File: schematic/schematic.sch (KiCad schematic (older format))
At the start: 19 parts, among them J1 Conn_01x04, J2 Conn_01x04, J3 Conn_01x04, J4 Conn_01x04, J5 Conn_01x04, SW1 SW_Push_Dual, U1 STM32F401VETx, Y1 Crystal_GND24

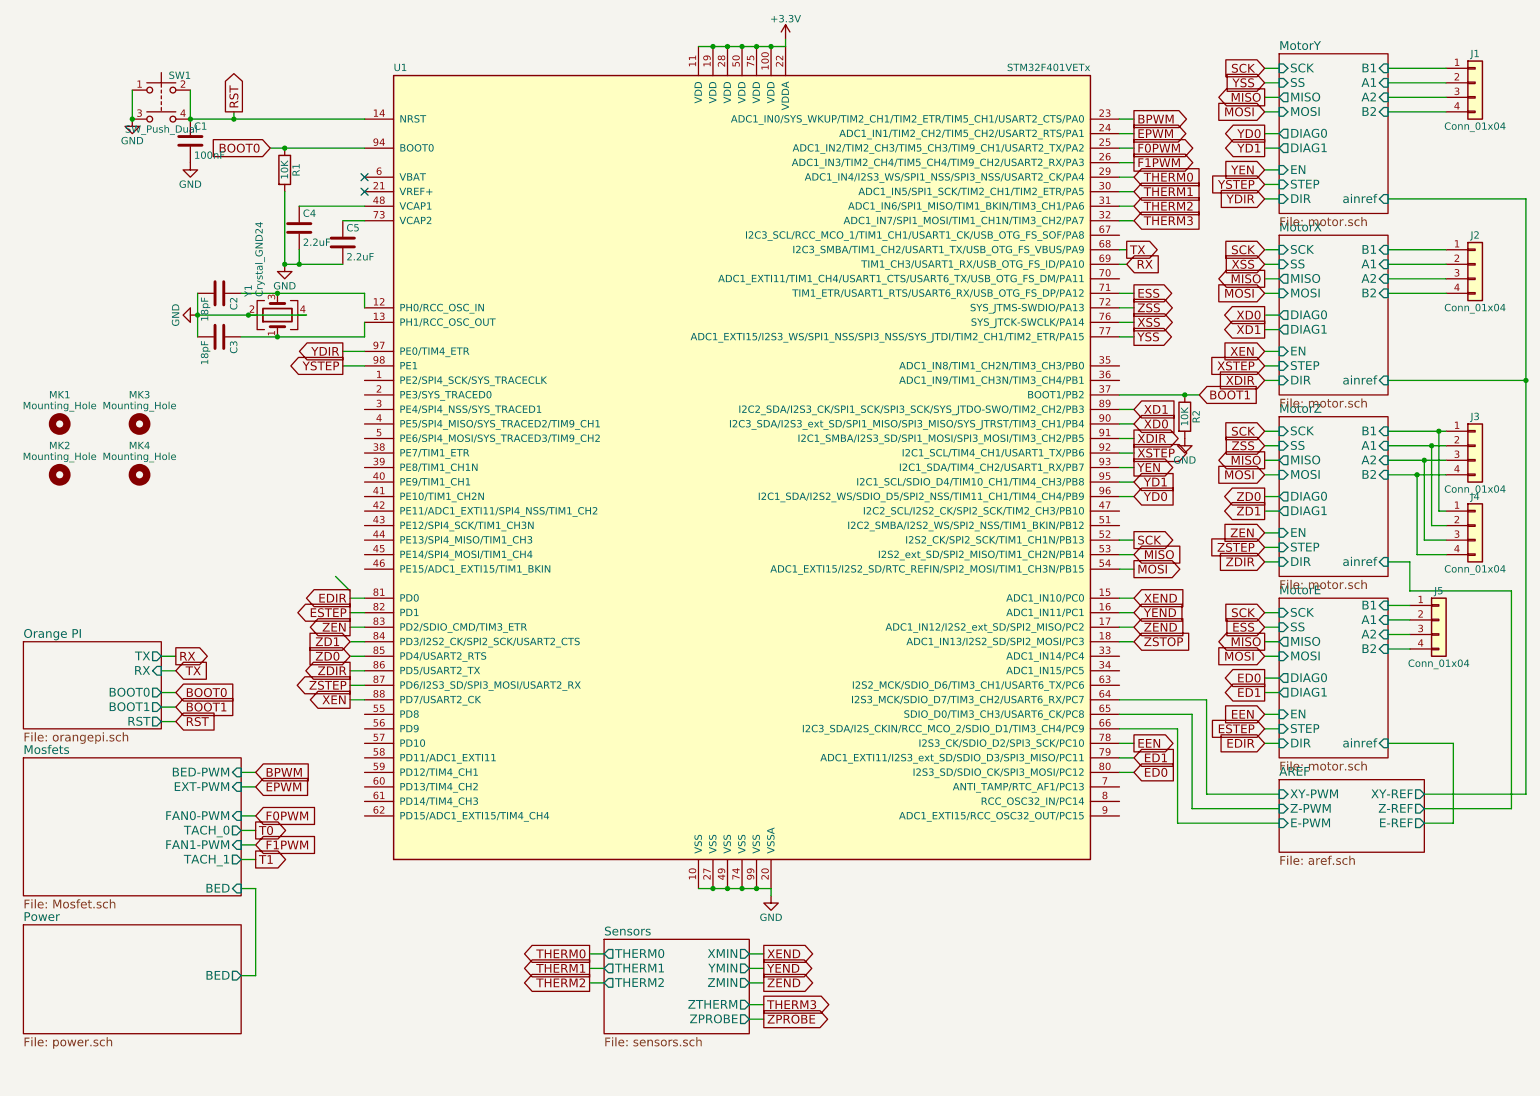
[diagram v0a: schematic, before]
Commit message: routed 3.3V power and start re arange signals
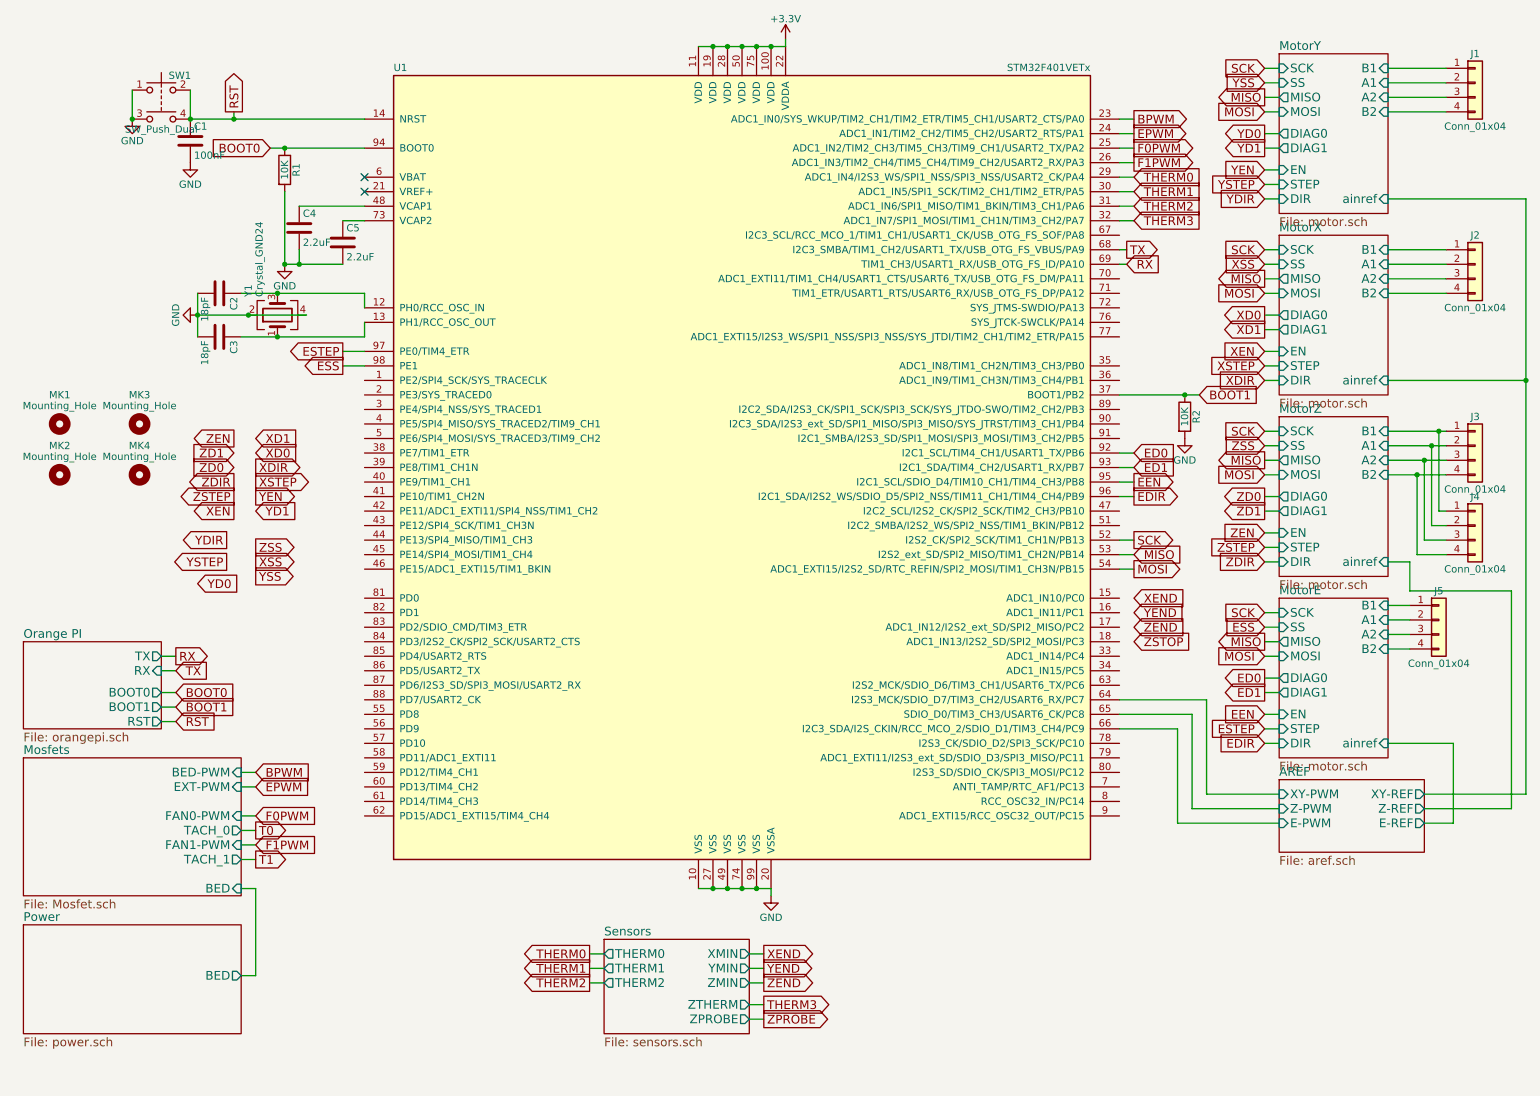
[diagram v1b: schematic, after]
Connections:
- net ED0: now also U1.92 (I2C1_SCL/TIM4_CH1/USART1_TX/PB6); no longer U1.80 (I2S3_SD/SDIO_CK/SPI3_MOSI/PC12)
- net ED1: now also U1.93 (I2C1_SDA/TIM4_CH2/USART1_RX/PB7); no longer U1.79 (ADC1_EXTI11/I2S3_ext_SD/SDIO_D3/SPI3_MISO/PC11)
- net EDIR: now also U1.96 (I2C1_SDA/I2S2_WS/SDIO_D5/SPI2_NSS/TIM11_CH1/TIM4_CH4/PB9); no longer U1.81 (PD0)
- net EEN: now also U1.95 (I2C1_SCL/SDIO_D4/TIM10_CH1/TIM4_CH3/PB8); no longer U1.78 (I2S3_CK/SDIO_D2/SPI3_SCK/PC10)
- net ESS: now also U1.98 (PE1); no longer U1.71 (TIM1_ETR/USART1_RTS/USART6_RX/USB_OTG_FS_DP/PA12)
- net ESTEP: now also U1.97 (PE0/TIM4_ETR); no longer U1.82 (PD1)
- net XD0: no longer U1.90 (I2C3_SDA/I2S3_ext_SD/SPI1_MISO/SPI3_MISO/SYS_JTRST/TIM3_CH1/PB4)
- net XD1: no longer U1.89 (I2C2_SDA/I2S3_CK/SPI1_SCK/SPI3_SCK/SYS_JTDO-SWO/TIM2_CH2/PB3)
- net XDIR: no longer U1.91 (I2C1_SMBA/I2S3_SD/SPI1_MOSI/SPI3_MOSI/TIM3_CH2/PB5)
- net XEN: no longer U1.88 (PD7/USART2_CK)
- net XEND: no longer U1.15 (ADC1_IN10/PC0)
- net XSS: no longer U1.76 (SYS_JTCK-SWCLK/PA14)
- net XSTEP: no longer U1.92 (I2C1_SCL/TIM4_CH1/USART1_TX/PB6)
- net YD0: no longer U1.96 (I2C1_SDA/I2S2_WS/SDIO_D5/SPI2_NSS/TIM11_CH1/TIM4_CH4/PB9)
- net YD1: no longer U1.95 (I2C1_SCL/SDIO_D4/TIM10_CH1/TIM4_CH3/PB8)
- net YDIR: no longer U1.97 (PE0/TIM4_ETR)
- net YEN: no longer U1.93 (I2C1_SDA/TIM4_CH2/USART1_RX/PB7)
- net YEND: no longer U1.16 (ADC1_IN11/PC1)
- net YSS: no longer U1.77 (ADC1_EXTI15/I2S3_WS/SPI1_NSS/SPI3_NSS/SYS_JTDI/TIM2_CH1/TIM2_ETR/PA15)
- net YSTEP: no longer U1.98 (PE1)
- net ZD0: no longer U1.85 (PD4/USART2_RTS)
- net ZD1: no longer U1.84 (PD3/I2S2_CK/SPI2_SCK/USART2_CTS)
- net ZDIR: no longer U1.86 (PD5/USART2_TX)
- net ZEN: no longer U1.83 (PD2/SDIO_CMD/TIM3_ETR)
- net ZEND: no longer U1.17 (ADC1_IN12/I2S2_ext_SD/SPI2_MISO/PC2)
- net ZSS: no longer U1.72 (SYS_JTMS-SWDIO/PA13)
- net ZSTEP: no longer U1.87 (PD6/I2S3_SD/SPI3_MOSI/USART2_RX)
- net ZSTOP: no longer U1.18 (ADC1_IN13/I2S2_SD/SPI2_MOSI/PC3)
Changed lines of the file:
@@
 LIBS:psmn1
 LIBS:tmc2130
+LIBS:schematic-cache
 EELAYER 25 0
 EELAYER END
@@
 Text GLabel 9100 1600 0    60   Input ~ 0
 YSTEP
-Text GLabel 2750 2850 0    60   Output ~ 0
+Text GLabel 1950 4200 0    60   Output ~ 0
 YSTEP
 Wire Wire Line
-	2900 2850 2750 2850
-Wire Wire Line
 	9100 1600 9200 1600
-Text GLabel 2750 2750 0    60   Output ~ 0
+Text GLabel 1950 4050 0    60   Output ~ 0
 YDIR
 Text GLabel 9100 1700 0    60   Input ~ 0
@@
 Wire Wire Line
 	9200 1700 9100 1700
-Wire Wire Line
-	2900 2750 2750 2750
 Text GLabel 9100 1250 0    60   Output ~ 0
 YD0
@@
 Wire Wire Line
 	9100 1250 9200 1250
-Text GLabel 8200 3750 2    60   Input ~ 0
+Text GLabel 1750 4350 2    60   Input ~ 0
 YD0
-Text GLabel 8200 3650 2    60   Input ~ 0
+Text GLabel 2150 3850 2    60   Input ~ 0
 YD1
-Text GLabel 8200 3550 2    60   Output ~ 0
+Text GLabel 2150 3750 2    60   Output ~ 0
 YEN
-Wire Wire Line
-	8100 3550 8200 3550
-Wire Wire Line
-	8100 3650 8200 3650
-Wire Wire Line
-	8100 3750 8200 3750
 Text GLabel 9100 2750 0    60   Input ~ 0
 XEN
@@
 Wire Wire Line
 	9100 3850 9200 3850
-Text GLabel 8200 3450 2    60   Output ~ 0
+Text GLabel 2150 3650 2    60   Output ~ 0
 XSTEP
-Text GLabel 8200 3350 2    60   Output ~ 0
+Text GLabel 2150 3550 2    60   Output ~ 0
 XDIR
-Text GLabel 8200 3250 2    60   Input ~ 0
+Text GLabel 2150 3450 2    60   Input ~ 0
 XD0
-Text GLabel 8200 3150 2    60   Input ~ 0
+Text GLabel 2150 3350 2    60   Input ~ 0
 XD1
-Text GLabel 2800 5150 0    60   Output ~ 0
+Text GLabel 2000 3850 0    60   Output ~ 0
 XEN
-Wire Wire Line
-	8100 3450 8200 3450
-Wire Wire Line
-	8100 3350 8200 3350
-Wire Wire Line
-	8100 3250 8200 3250
-Wire Wire Line
-	8100 3150 8200 3150
-Wire Wire Line
-	2800 5150 2900 5150
-Text GLabel 2800 5050 0    60   Output ~ 0
+Text GLabel 2000 3750 0    60   Output ~ 0
 ZSTEP
-Text GLabel 2800 4950 0    60   Output ~ 0
+Text GLabel 2000 3650 0    60   Output ~ 0
 ZDIR
-Text GLabel 2800 4850 0    60   Input ~ 0
+Text GLabel 2000 3550 0    60   Input ~ 0
 ZD0
-Text GLabel 2800 4750 0    60   Input ~ 0
+Text GLabel 2000 3450 0    60   Input ~ 0
 ZD1
-Text GLabel 2800 4650 0    60   Output ~ 0
+Text GLabel 2000 3350 0    60   Output ~ 0
 ZEN
-Wire Wire Line
-	2800 5050 2900 5050
-Wire Wire Line
-	2800 4950 2900 4950
-Wire Wire Line
-	2800 4850 2900 4850
-Wire Wire Line
-	2800 4750 2900 4750
-Wire Wire Line
-	2800 4650 2900 4650
-Text GLabel 2800 4550 0    60   Output ~ 0
+Text GLabel 2750 2750 0    60   Output ~ 0
 ESTEP
-Text GLabel 2800 4450 0    60   Output ~ 0
+Text GLabel 8200 3750 2    60   Output ~ 0
 EDIR
-Text GLabel 8200 5650 2    60   Input ~ 0
+Text GLabel 8200 3450 2    60   Input ~ 0
 ED0
-Text GLabel 8200 5550 2    60   Input ~ 0
+Text GLabel 8200 3550 2    60   Input ~ 0
 ED1
-Text GLabel 8200 5450 2    60   Output ~ 0
+Text GLabel 8200 3650 2    60   Output ~ 0
 EEN
-Wire Wire Line
-	8100 5650 8200 5650
-Wire Wire Line
-	8100 5550 8200 5550
-Wire Wire Line
-	8100 5450 8200 5450
-Wire Wire Line
-	2800 4450 2900 4450
-Wire Wire Line
-	2800 4550 2900 4550
 Wire Wire Line
 	2050 6450 2150 6450
@@
 Wire Wire Line
 	8100 4250 8200 4250
-Text GLabel 8200 2650 2    60   Output ~ 0
+Text GLabel 2150 4300 2    60   Output ~ 0
 YSS
-Text GLabel 8200 2550 2    60   Output ~ 0
+Text GLabel 2150 4200 2    60   Output ~ 0
 XSS
-Text GLabel 8200 2450 2    60   Output ~ 0
+Text GLabel 2150 4100 2    60   Output ~ 0
 ZSS
-Text GLabel 8200 2350 2    60   Output ~ 0
+Text GLabel 2750 2850 0    60   Output ~ 0
 ESS
-Wire Wire Line
-	8100 2650 8200 2650
-Wire Wire Line
-	8100 2550 8200 2550
-Wire Wire Line
-	8100 2450 8200 2450
-Wire Wire Line
-	8100 2350 8200 2350
 Wire Wire Line
 	8100 5150 8700 5150
@@
 Text GLabel 8200 4750 2    60   Input ~ 0
 ZSTOP
-Wire Wire Line
-	8100 4450 8200 4450
-Wire Wire Line
-	8100 4550 8200 4550
-Wire Wire Line
-	8100 4650 8200 4650
-Wire Wire Line
-	8100 4750 8200 4750
 Text GLabel 5650 6900 2    60   Output ~ 0
 XEND
@@
 	1750 2500 2500 2500
 Connection ~ 2100 2500
-Entry Wire Line
-	2700 4300 2800 4400
+Wire Wire Line
+	2900 2850 2750 2850
+Wire Wire Line
+	2750 2750 2900 2750
+Wire Wire Line
+	8100 3750 8200 3750
+Wire Wire Line
+	8100 3650 8200 3650
+Wire Wire Line
+	8200 3550 8100 3550
+Wire Wire Line
+	8100 3450 8200 3450
 $EndSCHEMATC

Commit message: Reassigned signals to driver for easier routing
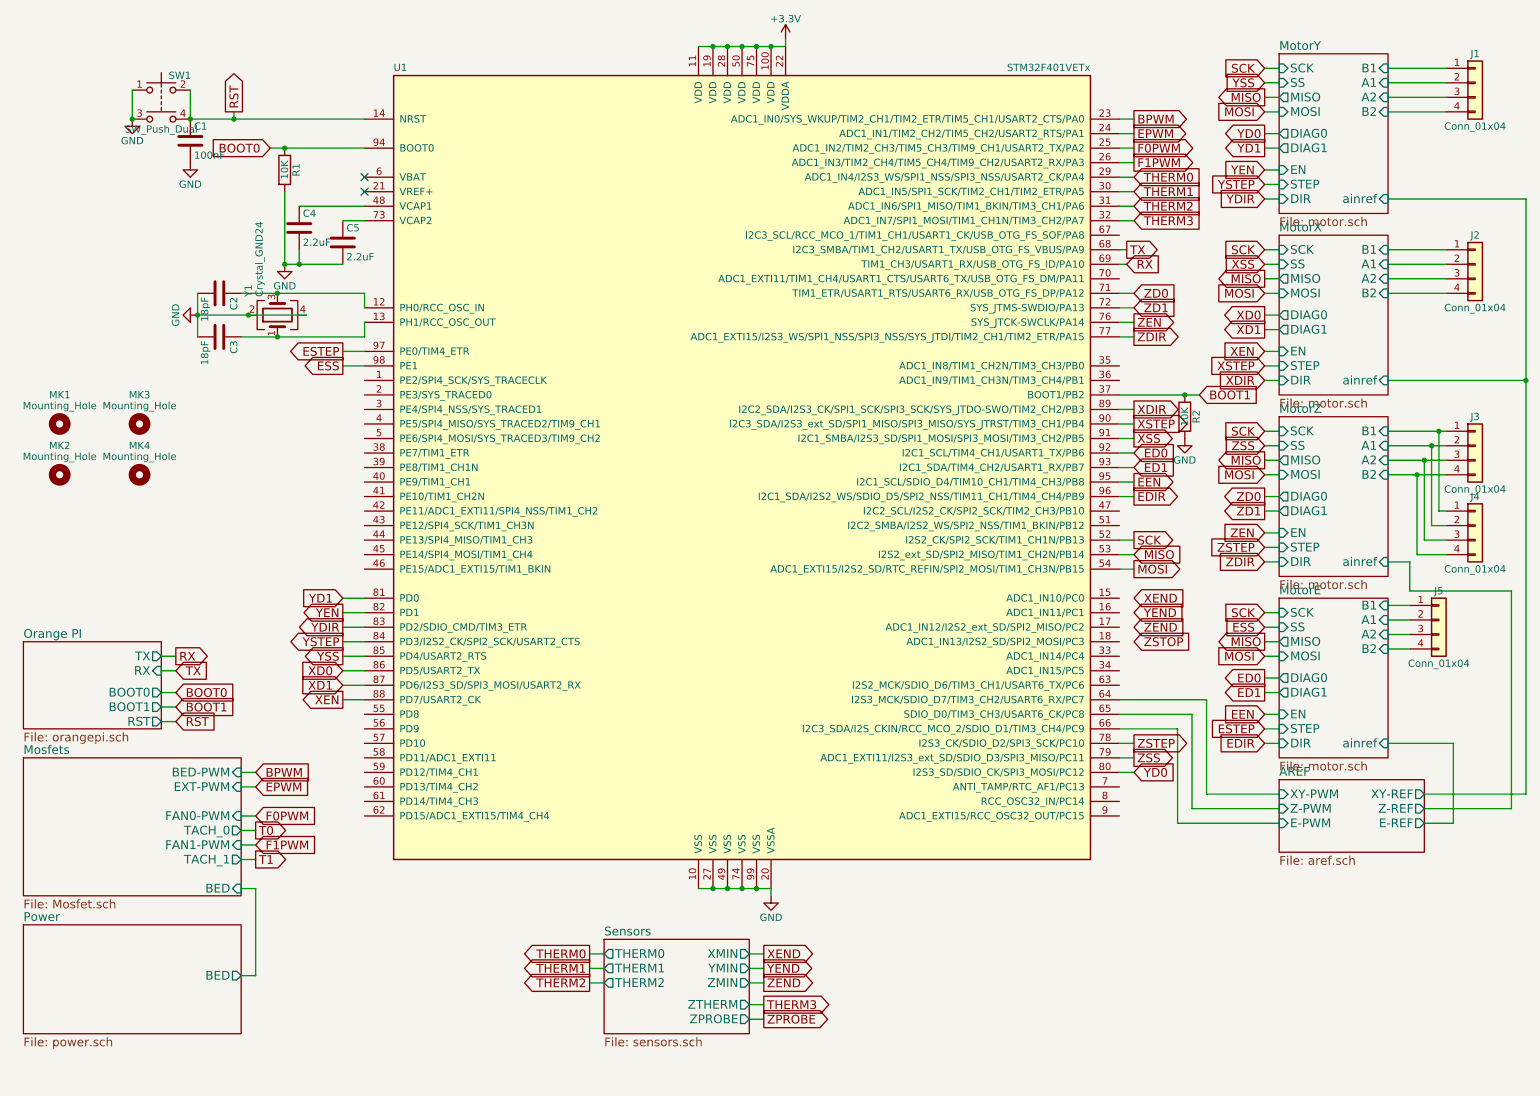
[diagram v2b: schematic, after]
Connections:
- net XD0: now also U1.86 (PD5/USART2_TX)
- net XD1: now also U1.87 (PD6/I2S3_SD/SPI3_MOSI/USART2_RX)
- net XDIR: now also U1.89 (I2C2_SDA/I2S3_CK/SPI1_SCK/SPI3_SCK/SYS_JTDO-SWO/TIM2_CH2/PB3)
- net XEN: now also U1.88 (PD7/USART2_CK)
- net XSS: now also U1.91 (I2C1_SMBA/I2S3_SD/SPI1_MOSI/SPI3_MOSI/TIM3_CH2/PB5)
- net XSTEP: now also U1.90 (I2C3_SDA/I2S3_ext_SD/SPI1_MISO/SPI3_MISO/SYS_JTRST/TIM3_CH1/PB4)
- net YD0: now also U1.80 (I2S3_SD/SDIO_CK/SPI3_MOSI/PC12)
- net YD1: now also U1.81 (PD0)
- net YDIR: now also U1.83 (PD2/SDIO_CMD/TIM3_ETR)
- net YEN: now also U1.82 (PD1)
- net YSS: now also U1.85 (PD4/USART2_RTS)
- net YSTEP: now also U1.84 (PD3/I2S2_CK/SPI2_SCK/USART2_CTS)
- net ZD0: now also U1.71 (TIM1_ETR/USART1_RTS/USART6_RX/USB_OTG_FS_DP/PA12)
- net ZD1: now also U1.72 (SYS_JTMS-SWDIO/PA13)
- net ZDIR: now also U1.77 (ADC1_EXTI15/I2S3_WS/SPI1_NSS/SPI3_NSS/SYS_JTDI/TIM2_CH1/TIM2_ETR/PA15)
- net ZEN: now also U1.76 (SYS_JTCK-SWCLK/PA14)
- net ZSS: now also U1.79 (ADC1_EXTI11/I2S3_ext_SD/SDIO_D3/SPI3_MISO/PC11)
- net ZSTEP: now also U1.78 (I2S3_CK/SDIO_D2/SPI3_SCK/PC10)
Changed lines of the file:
@@
 Text GLabel 9100 1600 0    60   Input ~ 0
 YSTEP
-Text GLabel 1950 4200 0    60   Output ~ 0
+Text GLabel 2750 4750 0    60   Output ~ 0
 YSTEP
 Wire Wire Line
 	9100 1600 9200 1600
-Text GLabel 1950 4050 0    60   Output ~ 0
+Text GLabel 2750 4650 0    60   Output ~ 0
 YDIR
 Text GLabel 9100 1700 0    60   Input ~ 0
@@
 Wire Wire Line
 	9100 1250 9200 1250
-Text GLabel 1750 4350 2    60   Input ~ 0
+Text GLabel 8200 5650 2    60   Input ~ 0
 YD0
-Text GLabel 2150 3850 2    60   Input ~ 0
+Text GLabel 2750 4450 0    60   Input ~ 0
 YD1
-Text GLabel 2150 3750 2    60   Output ~ 0
+Text GLabel 2750 4550 0    60   Output ~ 0
 YEN
 Text GLabel 9100 2750 0    60   Input ~ 0
@@
 Wire Wire Line
 	9100 3850 9200 3850
-Text GLabel 2150 3650 2    60   Output ~ 0
+Text GLabel 8200 3250 2    60   Output ~ 0
 XSTEP
-Text GLabel 2150 3550 2    60   Output ~ 0
+Text GLabel 8200 3150 2    60   Output ~ 0
 XDIR
-Text GLabel 2150 3450 2    60   Input ~ 0
+Text GLabel 2750 4950 0    60   Input ~ 0
 XD0
-Text GLabel 2150 3350 2    60   Input ~ 0
+Text GLabel 2750 5050 0    60   Input ~ 0
 XD1
-Text GLabel 2000 3850 0    60   Output ~ 0
+Text GLabel 2750 5150 0    60   Output ~ 0
 XEN
-Text GLabel 2000 3750 0    60   Output ~ 0
+Text GLabel 8200 5450 2    60   Output ~ 0
 ZSTEP
-Text GLabel 2000 3650 0    60   Output ~ 0
+Text GLabel 8200 2650 2    60   Output ~ 0
 ZDIR
-Text GLabel 2000 3550 0    60   Input ~ 0
+Text GLabel 8200 2350 2    60   Input ~ 0
 ZD0
-Text GLabel 2000 3450 0    60   Input ~ 0
+Text GLabel 8200 2450 2    60   Input ~ 0
 ZD1
-Text GLabel 2000 3350 0    60   Output ~ 0
+Text GLabel 8200 2550 2    60   Output ~ 0
 ZEN
 Text GLabel 2750 2750 0    60   Output ~ 0
@@
 Wire Wire Line
 	8100 4250 8200 4250
-Text GLabel 2150 4300 2    60   Output ~ 0
+Text GLabel 2750 4850 0    60   Output ~ 0
 YSS
-Text GLabel 2150 4200 2    60   Output ~ 0
+Text GLabel 8200 3350 2    60   Output ~ 0
 XSS
-Text GLabel 2150 4100 2    60   Output ~ 0
+Text GLabel 8200 5550 2    60   Output ~ 0
 ZSS
 Text GLabel 2750 2850 0    60   Output ~ 0
@@
 Wire Wire Line
 	8100 3450 8200 3450
+Wire Wire Line
+	8100 3350 8200 3350
+Wire Wire Line
+	8200 3250 8100 3250
+Wire Wire Line
+	8200 3150 8100 3150
+Wire Wire Line
+	2750 5150 2900 5150
+Wire Wire Line
+	2750 5050 2900 5050
+Wire Wire Line
+	2750 4950 2900 4950
+Wire Wire Line
+	2750 4850 2900 4850
+Wire Wire Line
+	2750 4750 2900 4750
+Wire Wire Line
+	2750 4650 2900 4650
+Wire Wire Line
+	2750 4550 2900 4550
+Wire Wire Line
+	2750 4450 2900 4450
+Wire Wire Line
+	8100 5650 8200 5650
+Wire Wire Line
+	8100 5550 8200 5550
+Wire Wire Line
+	8100 5450 8200 5450
+Wire Wire Line
+	8100 2650 8200 2650
+Wire Wire Line
+	8100 2550 8200 2550
+Wire Wire Line
+	8100 2350 8200 2350
+Wire Wire Line
+	8100 2450 8200 2450
 $EndSCHEMATC
